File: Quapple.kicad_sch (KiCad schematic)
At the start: 122 parts, among them J1 PC VIDEO IN, J2 MONITOR OUT, J3 COMP, J4 PADDLES, J5 TO SPEAKER, J6 FROM MOTHERBOARD, J7 PC_CTLR, P1 Conn_ISA_8bit, P2 EDGE_TO_DRIVES, P3 TO_DRIVES, Q1 2N3904, U1 TMS4164, U10 74LS161, U11 27C32, U12 74LS298, U13 74LS166, U14 74LS367, U15 74LS02, U16 74LS32, U17 74LS259, U18 74LS251, U19 NE558, U2 TMS4164, U20 TMS4164, U21 TMS4164, U22 TMS4164, U23 TMS4164, U24 TMS4416, U25 74LS373, U26 74LS245, U27 PAL16L8, U28 74LS161, U29 74LS161, U3 TMS4164, U30 PAL16L8, U31 74LS109, U32 74LS74, U33 PAL16R8, U34 PAL16L8, U35 74LS259, U36 74LS257, U37 74LS257, U38 74LS161, U39 74LS109, U4 TMS4164, U40 PAL16R4, U41 74LS38, U42 74LS194, U43 74LS02, U44 74LS04, U45 74LS194, U46 74LS257, U47 74LS257, U48 6502 (NMOS), U49 PAL16L8, U5 TMS4416, U50 PAL16R8, U51 PAL16L8, U52 74LS374, U53 74LS374, U54 74LS273, U55 74LS257, U56 74LS257, U6 74LS273, U7 PAL16R8, U8 PAL16L8, U9 74LS161

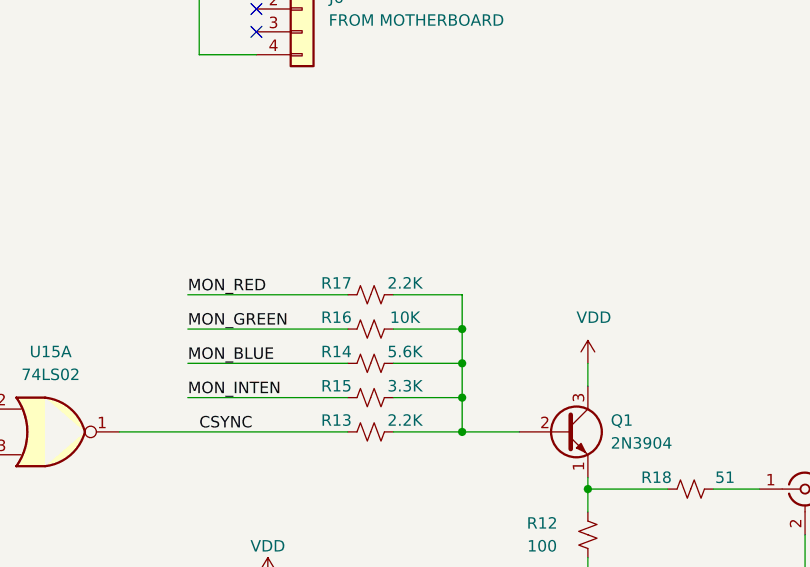
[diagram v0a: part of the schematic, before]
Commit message: Fix composite mode resistor
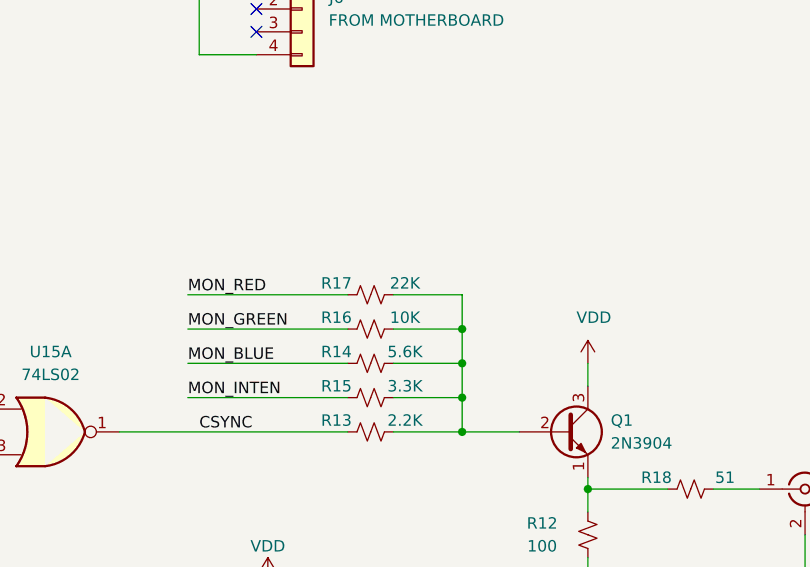
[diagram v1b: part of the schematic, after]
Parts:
- R17: value 2.2K -> 22K; Mouser 603-CFR-25JR-522K2 -> 603-CFR-25JR-5222K
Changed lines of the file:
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@@
     (in_bom yes) (on_board yes)
     (property "Reference" "R17" (id 0) (at 754.38 353.06 90))
-    (property "Value" "2.2K" (id 1) (at 762 353.06 90))
+    (property "Value" "22K" (id 1) (at 762 353.06 90))
     (property "Footprint" "Quapple:RES500" (id 2) (at 758.19 354.33 0)
       (effects (font (size 1.27 1.27)) hide)
@@
       (effects (font (size 1.27 1.27)) hide)
     )
-    (property "Mouser" "603-CFR-25JR-522K2" (id 4) (at 758.19 354.33 0)
+    (property "Mouser" "603-CFR-25JR-5222K" (id 4) (at 758.19 354.33 0)
       (effects (font (size 1.27 1.27)) hide)
     )
@@
     )
     (path "/8340b39a-6585-4750-961a-ab3a23e4c14f"
-      (reference "R17") (unit 1) (value "2.2K") (footprint "Quapple:RES500")
+      (reference "R17") (unit 1) (value "22K") (footprint "Quapple:RES500")
     )
     (path "/6579fc35-7e5e-4823-85c4-02931546b028"
